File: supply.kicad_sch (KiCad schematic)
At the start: 106 parts, among them J12 Molex_Nano-Fit-105430_xx02-ho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, Q11 PJE138K, Q13 BCM857BS-7-F, Q14 BCM857BS-7-F, Q15 SSM3J332R, Q16 SSM3J332R, Q18 SSM3J332R, Q5 PJE138K, Q6 SSM3J332R, Q7 PJE138K, Q8 PJE138K, SW1 PCM12SMTR, U1 TPS56C230, U29 TPS56C230, U37 74LVC2G14GV, U38 74LVC1G175GV, U41 NCP730BMT330TBG, U42 TPS7A0518PDBVT

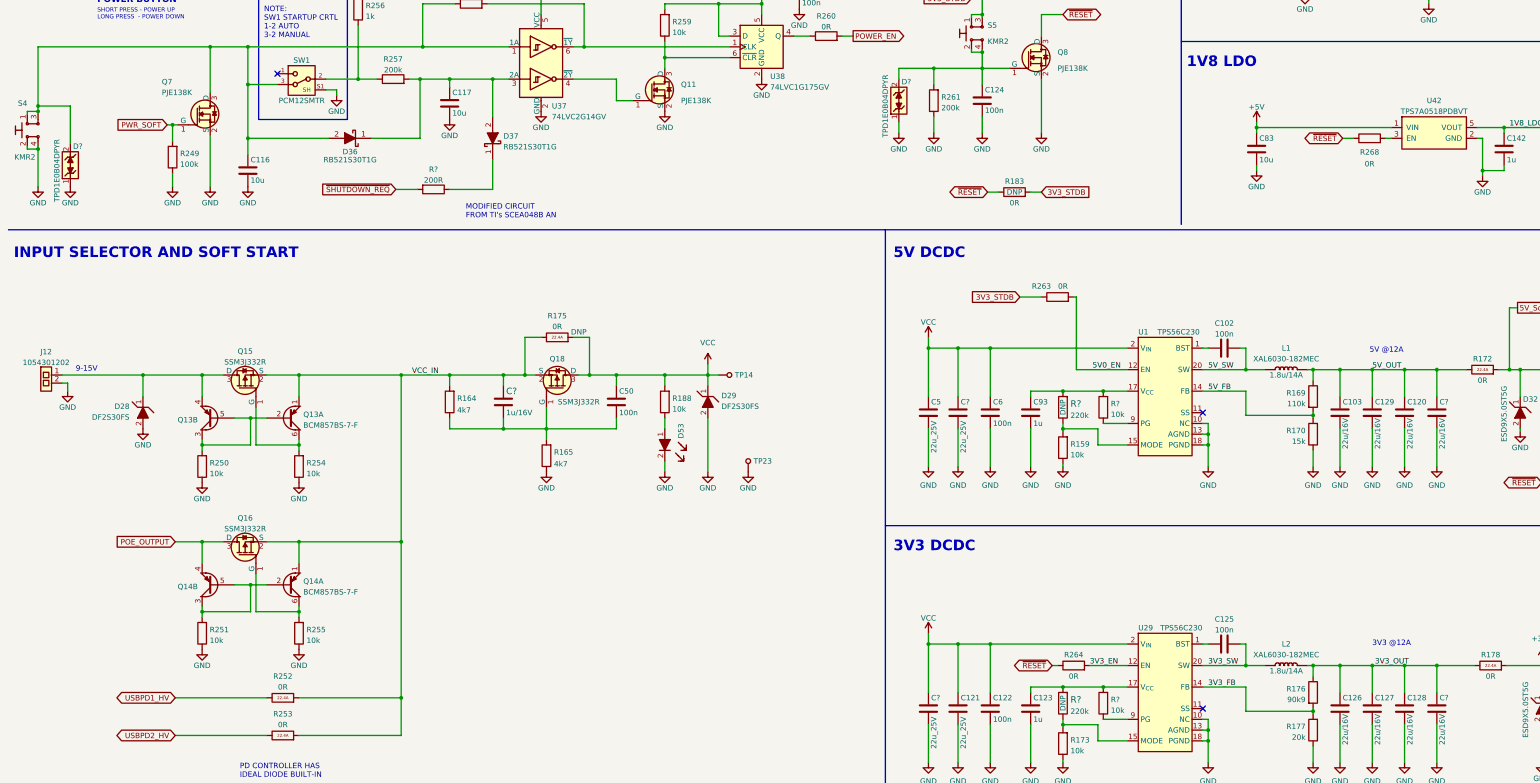
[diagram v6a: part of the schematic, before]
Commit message: Annotate parts, import them on PCB
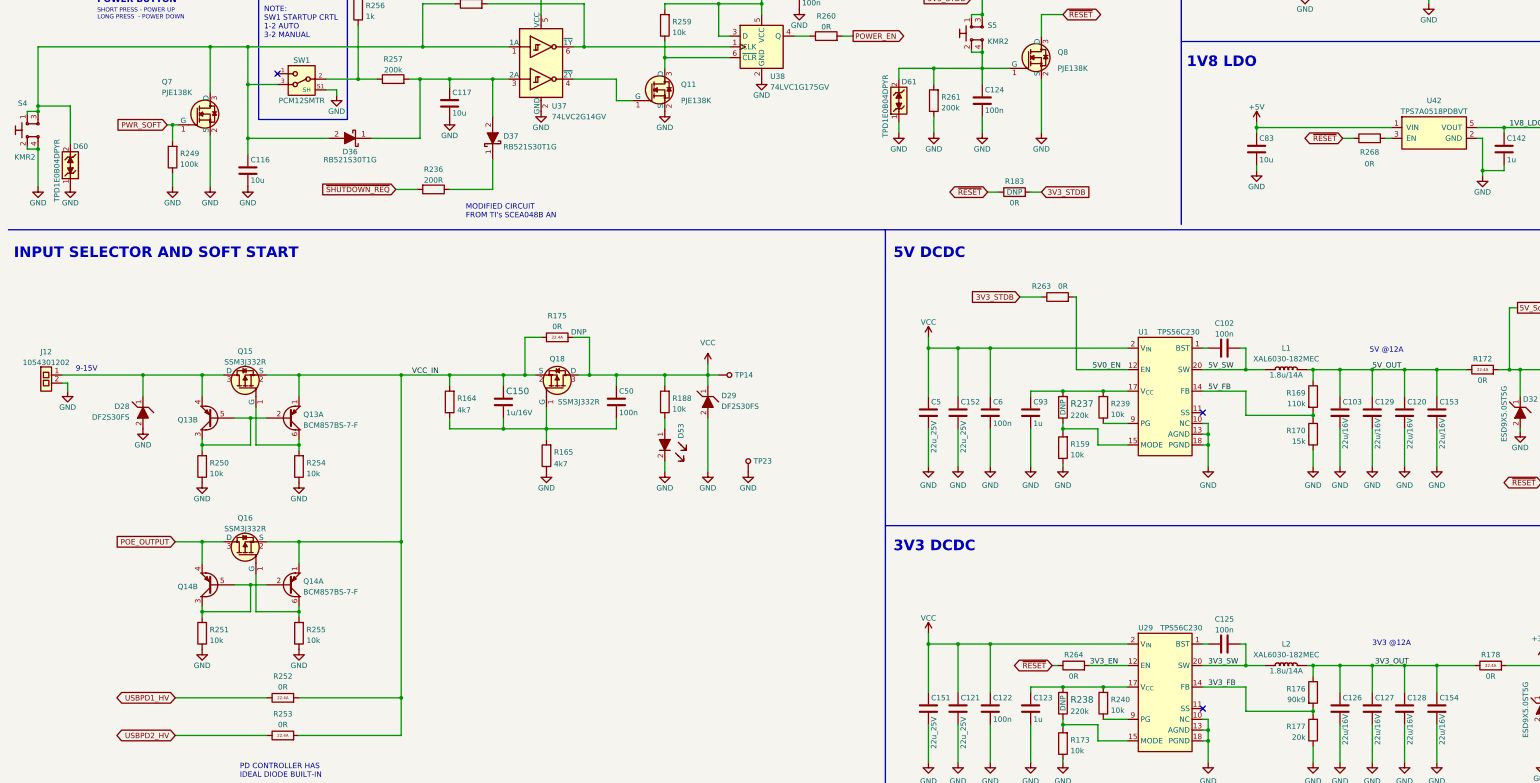
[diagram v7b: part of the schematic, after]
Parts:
- gave numbers to parts that had none: 12
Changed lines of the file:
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@@
   (symbol (lib_id "power:GND") (at 254 220.98 0) (unit 1)
     (in_bom yes) (on_board yes) (fields_autoplaced)
-    (property "Reference" "#PWR?" (id 0) (at 254 227.33 0)
+    (property "Reference" "#PWR0345" (id 0) (at 254 227.33 0)
       (effects (font (size 1.27 1.27)) hide)
     )
@@
   (symbol (lib_id "power:GND") (at 349.885 220.98 0) (unit 1)
     (in_bom yes) (on_board yes) (fields_autoplaced)
-    (property "Reference" "#PWR?" (id 0) (at 349.885 227.33 0)
+    (property "Reference" "#PWR0341" (id 0) (at 349.885 227.33 0)
       (effects (font (size 1.27 1.27)) hide)
     )
@@
   (symbol (lib_id "antmicroCapacitors0603:C_22u_0603_16V") (at 349.885 138.43 0) (unit 1)
     (in_bom yes) (on_board yes)
-    (property "Reference" "C?" (id 0) (at 350.52 135.89 0)
+    (property "Reference" "C153" (id 0) (at 350.52 135.89 0)
       (effects (font (size 1.27 1.27)) (justify left))
     )
@@
   (symbol (lib_id "antmicroResistors0402:R_220k_0402") (at 261.62 207.01 90) (unit 1)
     (in_bom yes) (on_board yes)
-    (property "Reference" "R?" (id 0) (at 263.398 206.1754 90)
+    (property "Reference" "R238" (id 0) (at 263.398 206.1754 90)
       (effects (font (size 1.524 1.524)) (justify right))
     )
@@
   (symbol (lib_id "jetson-orin-baseboard:R_10k_0402") (at 271.145 137.16 90) (unit 1)
     (in_bom yes) (on_board yes) (fields_autoplaced)
-    (property "Reference" "R?" (id 0) (at 272.923 136.3253 90)
+    (property "Reference" "R239" (id 0) (at 272.923 136.3253 90)
       (effects (font (size 1.27 1.27)) (justify right))
     )
@@
   (symbol (lib_id "power:GND") (at 342.265 220.98 0) (unit 1)
     (in_bom yes) (on_board yes) (fields_autoplaced)
-    (property "Reference" "#PWR?" (id 0) (at 342.265 227.33 0)
+    (property "Reference" "#PWR0340" (id 0) (at 342.265 227.33 0)
       (effects (font (size 1.27 1.27)) hide)
     )
@@
   (symbol (lib_id "jetson-orin-baseboard:TPD1E0B04DPYR ") (at 222.885 64.77 90) (unit 1)
     (in_bom yes) (on_board yes)
-    (property "Reference" "D?" (id 0) (at 223.52 60.325 90)
+    (property "Reference" "D61" (id 0) (at 223.52 60.325 90)
       (effects (font (size 1.27 1.27)) (justify right))
     )
@@
   (symbol (lib_id "power:GND") (at 236.855 151.13 0) (unit 1)
     (in_bom yes) (on_board yes) (fields_autoplaced)
-    (property "Reference" "#PWR?" (id 0) (at 236.855 157.48 0)
+    (property "Reference" "#PWR0352" (id 0) (at 236.855 157.48 0)
       (effects (font (size 1.27 1.27)) hide)
     )
@@
   (symbol (lib_id "power:GND") (at 349.885 151.13 0) (unit 1)
     (in_bom yes) (on_board yes) (fields_autoplaced)
-    (property "Reference" "#PWR?" (id 0) (at 349.885 157.48 0)
+    (property "Reference" "#PWR0339" (id 0) (at 349.885 157.48 0)
       (effects (font (size 1.27 1.27)) hide)
     )
@@
   (symbol (lib_id "power:GND") (at 244.475 220.98 0) (unit 1)
     (in_bom yes) (on_board yes) (fields_autoplaced)
-    (property "Reference" "#PWR?" (id 0) (at 244.475 227.33 0)
+    (property "Reference" "#PWR0348" (id 0) (at 244.475 227.33 0)
       (effects (font (size 1.27 1.27)) hide)
     )
@@
   (symbol (lib_id "antmicroCapacitorsmisc:C_22u_0805_25V") (at 229.87 208.28 0) (mirror y) (unit 1)
     (in_bom yes) (on_board yes)
-    (property "Reference" "C?" (id 0) (at 230.505 205.74 0)
+    (property "Reference" "C151" (id 0) (at 230.505 205.74 0)
       (effects (font (size 1.27 1.27)) (justify right))
     )
@@
   (symbol (lib_id "antmicroCapacitorsmisc:C_22u_0805_25V") (at 236.855 138.43 0) (mirror y) (unit 1)
     (in_bom yes) (on_board yes)
-    (property "Reference" "C?" (id 0) (at 237.49 135.89 0)
+    (property "Reference" "C152" (id 0) (at 237.49 135.89 0)
       (effects (font (size 1.27 1.27)) (justify right))
     )
@@
   (symbol (lib_id "jetson-orin-baseboard:VCC") (at 229.87 190.5 0) (unit 1)
     (in_bom yes) (on_board yes) (fields_autoplaced)
-    (property "Reference" "#PWR?" (id 0) (at 229.87 194.31 0)
+    (property "Reference" "#PWR0338" (id 0) (at 229.87 194.31 0)
       (effects (font (size 1.27 1.27)) hide)
     )
@@
   (symbol (lib_id "power:GND") (at 295.91 220.98 0) (unit 1)
     (in_bom yes) (on_board yes) (fields_autoplaced)
-    (property "Reference" "#PWR?" (id 0) (at 295.91 227.33 0)
+    (property "Reference" "#PWR0347" (id 0) (at 295.91 227.33 0)
       (effects (font (size 1.27 1.27)) hide)
     )
@@
   (symbol (lib_id "power:GND") (at 236.855 220.98 0) (unit 1)
     (in_bom yes) (on_board yes) (fields_autoplaced)
-    (property "Reference" "#PWR?" (id 0) (at 236.855 227.33 0)
+    (property "Reference" "#PWR0349" (id 0) (at 236.855 227.33 0)
       (effects (font (size 1.27 1.27)) hide)
     )
@@
   (symbol (lib_id "power:GND") (at 327.025 220.98 0) (unit 1)
     (in_bom yes) (on_board yes) (fields_autoplaced)
-    (property "Reference" "#PWR?" (id 0) (at 327.025 227.33 0)
+    (property "Reference" "#PWR0343" (id 0) (at 327.025 227.33 0)
       (effects (font (size 1.27 1.27)) hide)
     )
@@
   (symbol (lib_id "antmicroResistors0402:R_220k_0402") (at 261.62 137.16 90) (unit 1)
     (in_bom yes) (on_board yes)
-    (property "Reference" "R?" (id 0) (at 263.398 136.3254 90)
+    (property "Reference" "R237" (id 0) (at 263.398 136.3254 90)
       (effects (font (size 1.524 1.524)) (justify right))
     )
@@
   (symbol (lib_id "power:GND") (at 229.87 220.98 0) (unit 1)
     (in_bom yes) (on_board yes) (fields_autoplaced)
-    (property "Reference" "#PWR?" (id 0) (at 229.87 227.33 0)
+    (property "Reference" "#PWR0350" (id 0) (at 229.87 227.33 0)
       (effects (font (size 1.27 1.27)) hide)
     )
@@
   (symbol (lib_id "power:GND") (at 261.62 220.98 0) (unit 1)
     (in_bom yes) (on_board yes) (fields_autoplaced)
-    (property "Reference" "#PWR?" (id 0) (at 261.62 227.33 0)
+    (property "Reference" "#PWR0346" (id 0) (at 261.62 227.33 0)
       (effects (font (size 1.27 1.27)) hide)
     )
@@
   (symbol (lib_id "power:GND") (at 222.885 72.39 0) (unit 1)
     (in_bom yes) (on_board yes)
-    (property "Reference" "#PWR?" (id 0) (at 222.885 78.74 0)
+    (property "Reference" "#PWR0351" (id 0) (at 222.885 78.74 0)
       (effects (font (size 1.27 1.27)) hide)
     )
@@
   (symbol (lib_id "power:GND") (at 320.675 220.98 0) (unit 1)
     (in_bom yes) (on_board yes) (fields_autoplaced)
-    (property "Reference" "#PWR?" (id 0) (at 320.675 227.33 0)
+    (property "Reference" "#PWR0344" (id 0) (at 320.675 227.33 0)
       (effects (font (size 1.27 1.27)) hide)
     )
@@
   (symbol (lib_id "antmicroCapacitors0603:C_22u_0603_16V") (at 349.885 208.28 0) (unit 1)
     (in_bom yes) (on_board yes)
-    (property "Reference" "C?" (id 0) (at 350.52 205.74 0)
+    (property "Reference" "C154" (id 0) (at 350.52 205.74 0)
       (effects (font (size 1.27 1.27)) (justify left))
     )
@@
   (symbol (lib_id "power:GND") (at 27.305 85.09 0) (unit 1)
     (in_bom yes) (on_board yes)
-    (property "Reference" "#PWR?" (id 0) (at 27.305 91.44 0)
+    (property "Reference" "#PWR0337" (id 0) (at 27.305 91.44 0)
       (effects (font (size 1.27 1.27)) hide)
     )
@@
   (symbol (lib_id "antmicroCapacitors0402:C_1u_0402_16V") (at 129.54 135.89 0) (unit 1)
     (in_bom yes) (on_board yes)
-    (property "Reference" "C?" (id 0) (at 130.175 133.35 0)
+    (property "Reference" "C150" (id 0) (at 130.175 133.35 0)
       (effects (font (size 1.524 1.524)) (justify left))
     )
@@
   (symbol (lib_id "jetson-orin-baseboard:R_200R_0402") (at 113.03 85.725 180) (unit 1)
     (in_bom yes) (on_board yes) (fields_autoplaced)
-    (property "Reference" "R?" (id 0) (at 113.03 81.0092 0))
+    (property "Reference" "R236" (id 0) (at 113.03 81.0092 0))
     (property "Value" "R_200R_0402" (id 1) (at 113.03 81.915 0)
       (effects (font (size 1.27 1.27)) hide)
@@
   (symbol (lib_id "power:GND") (at 334.645 220.98 0) (unit 1)
     (in_bom yes) (on_board yes) (fields_autoplaced)
-    (property "Reference" "#PWR?" (id 0) (at 334.645 227.33 0)
+    (property "Reference" "#PWR0342" (id 0) (at 334.645 227.33 0)
       (effects (font (size 1.27 1.27)) hide)
     )
@@
   (symbol (lib_id "jetson-orin-baseboard:TPD1E0B04DPYR ") (at 27.305 80.01 90) (unit 1)
     (in_bom yes) (on_board yes)
-    (property "Reference" "D?" (id 0) (at 27.94 75.565 90)
+    (property "Reference" "D60" (id 0) (at 27.94 75.565 90)
       (effects (font (size 1.27 1.27)) (justify right))
     )
@@
   (symbol (lib_id "jetson-orin-baseboard:R_10k_0402") (at 271.145 207.01 90) (unit 1)
     (in_bom yes) (on_board yes) (fields_autoplaced)
-    (property "Reference" "R?" (id 0) (at 272.923 206.1753 90)
+    (property "Reference" "R240" (id 0) (at 272.923 206.1753 90)
       (effects (font (size 1.27 1.27)) (justify right))
     )

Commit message: Loclib
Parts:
- C103, C120, C126, C127, C128, C129, C153, C154: footprint antmicro-footprints:0603-cap -> jetson-orin-baseboard-footprints:0603-cap; symbol antmicroCapacitors0603:C_22u_0603_16V -> jetson-orin-baseboard:C_22u_0603_16V
- C121, C151, C152, C5: footprint antmicro-footprints:0805-cap -> jetson-orin-baseboard-footprints:0805-cap; symbol antmicroCapacitorsmisc:C_22u_0805_25V -> jetson-orin-baseboard:C_22u_0805_25V
- C150: footprint antmicro-footprints:0402-cap -> jetson-orin-baseboard-footprints:0402-cap; symbol antmicroCapacitors0402:C_1u_0402_16V -> jetson-orin-baseboard:C_1u_0402_16V
- L1, L2: footprint antmicro-footprints:Coilcraft-XAL6030 -> jetson-orin-baseboard-footprints:Coilcraft-XAL6030; symbol antmicroFixedInductors:XAL6030-182MEC -> jetson-orin-baseboard:XAL6030-182MEC
- Q11, Q5, Q7, Q8: footprint antmicro-footprints:SOT-523 -> jetson-orin-baseboard-footprints:SOT-523; symbol antmicroTransistorsFETsMOSFETsSingle:PJE138K -> jetson-orin-baseboard:PJE138K
- R169: footprint antmicro-footprints:0402-res -> jetson-orin-baseboard-footprints:0402-res; symbol antmicroResistors0402:R_110k_0402 -> jetson-orin-baseboard:R_110k_0402
- R170: footprint antmicro-footprints:0402-res -> jetson-orin-baseboard-footprints:0402-res; symbol antmicroResistors0402:R_15k_0402 -> jetson-orin-baseboard:R_15k_0402
- R172, R175, R178, R182, R252, R253: footprint antmicro-footprints:0603-res -> jetson-orin-baseboard-footprints:0603-res; symbol antmicroResistors0603:R_0R_0603_HPWR -> jetson-orin-baseboard:R_0R_0603_HPWR
- R176: footprint antmicro-footprints:0402-res -> jetson-orin-baseboard-footprints:0402-res; symbol antmicroResistors0402:R_90k9_0402 -> jetson-orin-baseboard:R_90k9_0402
- R177: footprint antmicro-footprints:0402-res -> jetson-orin-baseboard-footprints:0402-res; symbol antmicroResistors0402:R_20k_0402 -> jetson-orin-baseboard:R_20k_0402
- R237, R238: footprint antmicro-footprints:0402-res -> jetson-orin-baseboard-footprints:0402-res; symbol antmicroResistors0402:R_220k_0402 -> jetson-orin-baseboard:R_220k_0402
- S4, S5: footprint antmicro-footprints:SW_SPST_4.2x2.8 -> jetson-orin-baseboard-footprints:SW_SPST_4.2x2.8; symbol antmicroPushbuttonSwitches:KMR2 -> jetson-orin-baseboard:KMR2
- U1, U29: footprint antmicro-footprints:QFN-20_EP_3x3_Pitch0.45mm -> jetson-orin-baseboard-footprints:QFN-20_EP_3x3_Pitch0.45mm; symbol antmicroDCDCConverters:TPS56C230 -> jetson-orin-baseboard:TPS56C230
